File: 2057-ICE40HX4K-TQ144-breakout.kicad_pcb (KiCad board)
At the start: 2 copper layers, 99.1 x 66 mm, 61 parts, among them J1 Conn_02x30_Odd_Even, J2 Conn_02x30_Odd_Even, J3 RaspberryPI-B+header, J4 0548190519, J5 RaspberryPI-B+header, J6 Conn_02x07_Odd_Even, J7 Conn_02x01, U1 ICE40HX4K-TQ144, U2 AZ1117CH-3.3TRG1, U3 AZ1117CH-1.2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

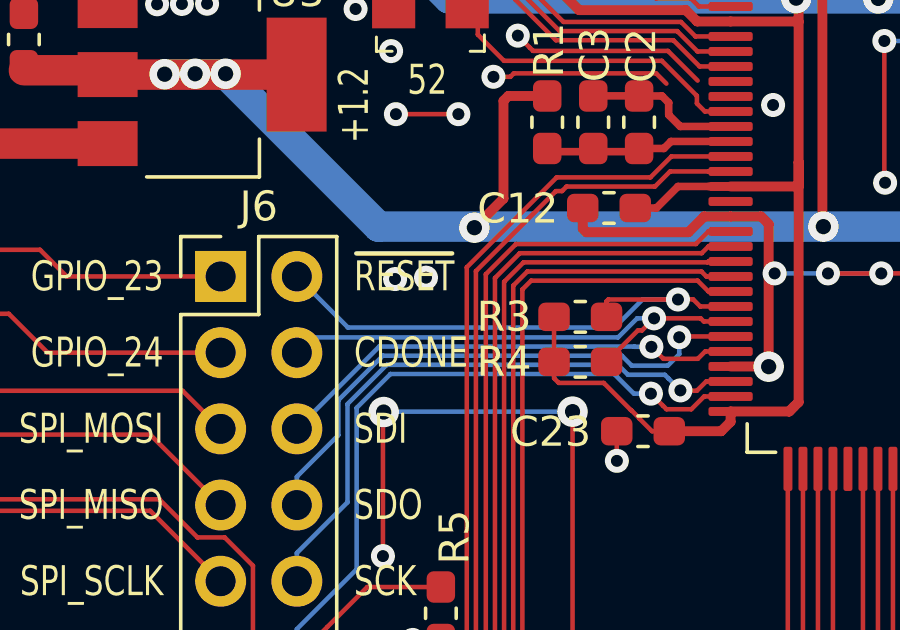
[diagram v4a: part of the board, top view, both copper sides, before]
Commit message: swap ~reset & cdone on silkscreen :-/
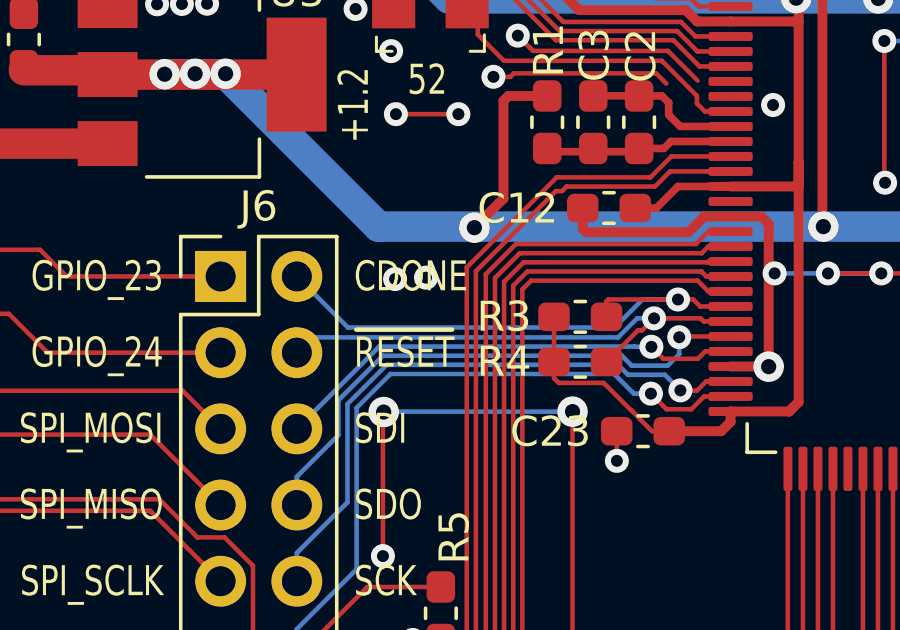
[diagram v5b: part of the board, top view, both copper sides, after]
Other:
- board text added: "~RESET"
- board text removed: "~RESET~"
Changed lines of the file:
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@@
-(kicad_pcb (version 20171130) (host pcbnew 5.1.5-52549c5~84~ubuntu18.04.1)
+(kicad_pcb (version 20171130) (host pcbnew 5.1.5+dfsg1-2build2)
   (general
     (thickness 1.6)
@@
     (effects (font (size 1 0.762) (thickness 0.15)))
   )
-  (gr_text CDONE (at 69.215 77.47) (layer F.SilkS)
+  (gr_text CDONE (at 69.215 74.93) (layer F.SilkS)
     (effects (font (size 1 0.762) (thickness 0.15)) (justify left))
   )
-  (gr_text ~RESET~ (at 69.215 74.93) (layer F.SilkS)
+  (gr_text ~RESET (at 69.215 77.47) (layer F.SilkS)
     (effects (font (size 1 0.762) (thickness 0.15)) (justify left))
   )

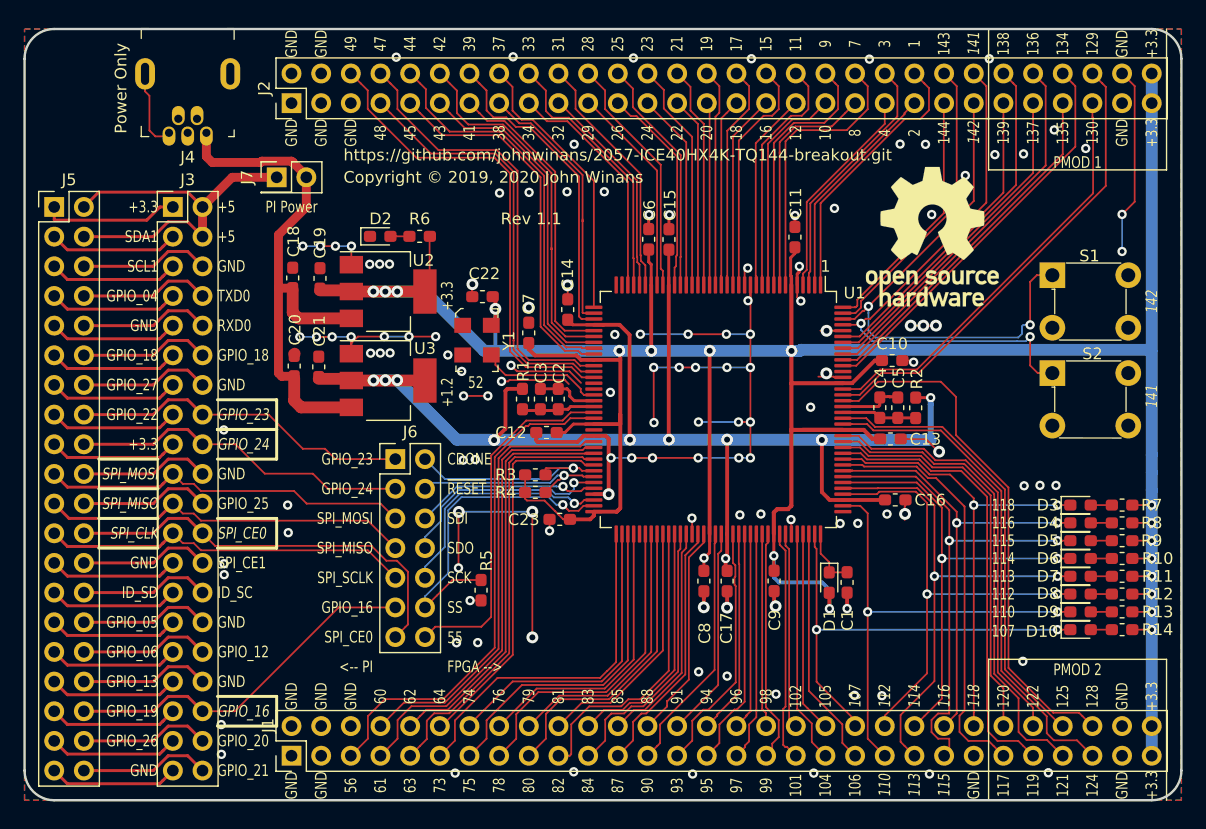
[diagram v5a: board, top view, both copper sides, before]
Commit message: Add FLASH, SD, gnd testpoints for Rev 2.0
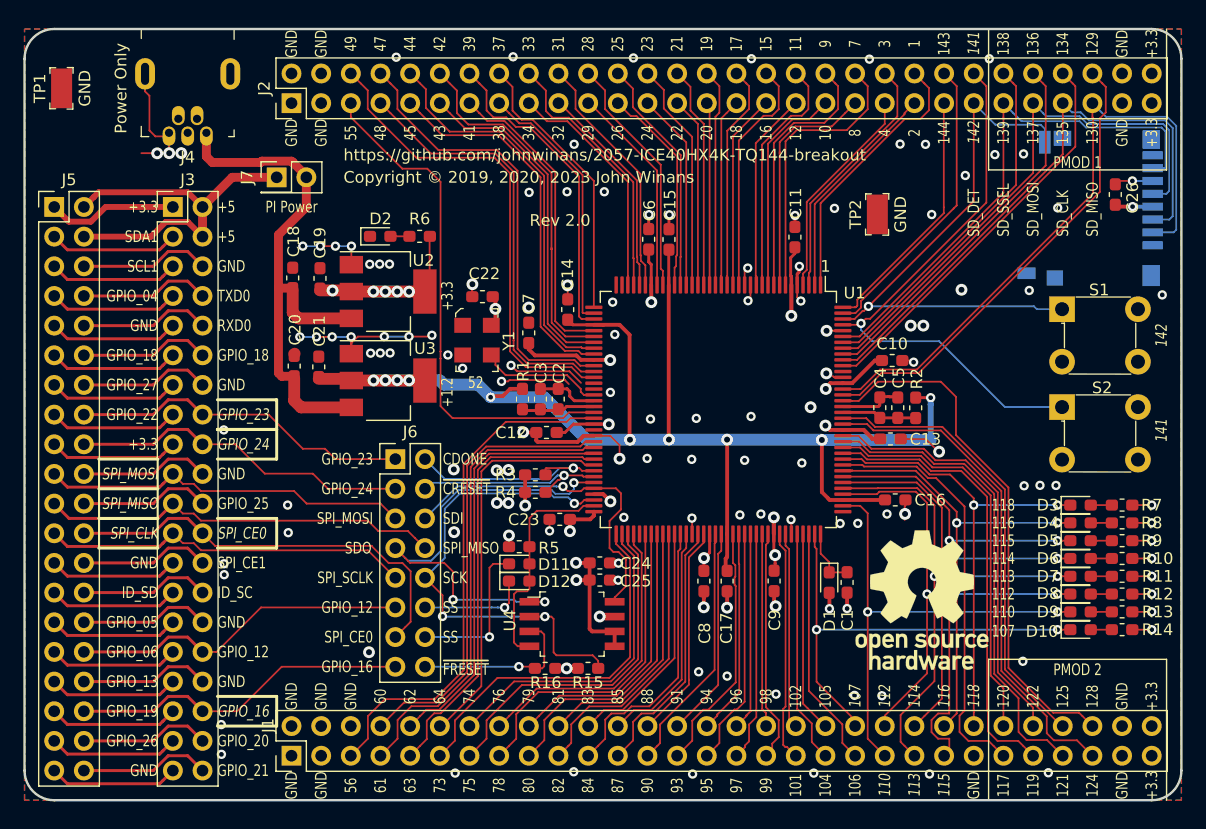
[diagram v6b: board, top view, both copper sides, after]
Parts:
- added C24: .1uF, Capacitor_SMD:C_0603_1608Metric_Pad1.05x0.95mm_HandSolder, F.Cu at (82.3, 83.8)
- added C25: 4.7uF, Capacitor_SMD:C_0603_1608Metric_Pad1.05x0.95mm_HandSolder, F.Cu at (82.3, 85.3)
- added C26: .1uF, Capacitor_SMD:C_0603_1608Metric_Pad1.05x0.95mm_HandSolder, F.Cu at (126.4, 52.3)
- added D11: 1N4448WSF-7, Diode_SMD:D_0603_1608Metric_Pad1.05x0.95mm_HandSolder, F.Cu at (75.4, 83.9)
- added D12: 1N4448WSF-7, Diode_SMD:D_0603_1608Metric_Pad1.05x0.95mm_HandSolder, F.Cu at (75.4, 85.4)
- added J8: Micro_SD_Card_Det, jb-footprint:microSD_HC_Hirose_DM3D-SF-bigpad, B.Cu at (124.3, 53.4)
- added R15: 10K, Resistor_SMD:R_0603_1608Metric_Pad1.05x0.95mm_HandSolder, F.Cu at (81.3, 92.8)
- added R16: 10K, Resistor_SMD:R_0603_1608Metric_Pad1.05x0.95mm_HandSolder, F.Cu at (77.6, 92.8)
- added TP1: RCW-0C, digikey-footprints:PROBE_PAD_1206, F.Cu at (36.2, 43.2)
- added TP2: RCW-0C, digikey-footprints:PROBE_PAD_1206, F.Cu at (106.0, 54.0)
- added U4: AT45DB161D-SU, digikey-footprints:SOIC-8_W5.6mm, F.Cu at (79.9, 89.0)
- D1: value D_ALT -> 1N4448WSF-7
- J6: value Conn_02x07_Odd_Even -> Conn_02x08_Odd_Even; footprint Connector_PinHeader_2.54mm:PinHeader_2x07_P2.54mm_Vertical -> Connector_PinHeader_2.54mm:PinHeader_2x08_P2.54mm_Vertical
- moved LOGO1 31.1 mm to (109.9, 87.0)
- moved R5 4.96 mm to (75.4, 82.4), turned to 180 degrees
- moved S2 3.03 mm to (121.9, 70.5)
- moved S1 3.03 mm to (121.9, 62.1)
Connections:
- J2 pad 5: GND -> /IOB_91
- J6 pad 11: /GPIO16 -> /GPIO12
- J6 pad 12: /IOB_108_SS -> /J6_GPIO12
- J6 pad 14: /IOB_91 -> /J6_CE0
- J6 pad 7: /SPI_MISO -> /IOB_105_SDO
- J6 pad 8: /IOB_105_SDO -> /SPI_MISO
- R5 pad 1: GND -> /IOB_108_SS
- R5 pad 2: /IOB_108_SS -> +3V3
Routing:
- net +3V3: track 288.2 -> 99.3 mm, vias 19 -> 31
- net GND: track 272.8 -> 183.8 mm, vias 129 -> 122
- net /IOB_107_SCK: track 20.4 -> 42.9 mm, vias 1 -> 3
- net /IOB_105_SDO: track 18.6 -> 40.4 mm, vias 1 -> 3
- net /IOT_213: track 30.5 -> 50.2 mm
- net /IOT_215: track 28.5 -> 47.8 mm
- net /IOT_217: track 26.5 -> 45.6 mm
- net /IOT_206: track 36.1 -> 55.1 mm
- net /GPIO12: track 11.2 -> 29.3 mm
- net /~FRESET~: track 0.00 -> 14.4 mm, vias 0 -> 1
- net /IOB_91: track 30.5 -> 44.1 mm
- net /IOB_106_SDI: track 15.9 -> 29.3 mm
- net /J6_CE0: track 0.00 -> 13.3 mm, vias 0 -> 1
- net /IOB_108_SS: track 28.5 -> 19.1 mm, vias 1 -> 0
- net /J6_GPIO12: track 0.00 -> 9.25 mm, vias 0 -> 1
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- added copper zone on In2.Cu, net +3V3
- added copper zone on In1.Cu, net GND
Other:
- copper layers 2 -> 4
- board text added: "Copyright © 2019, 2020, 2023 John Winans"
- board text added: "Rev 2.0"
- board text added: "SD_CLK"
- board text added: "SD_DET"
- board text added: "SD_MISO"
- board text added: "SD_MOSI"
- board text added: "SD_SSEL"
- board text added: "https://github.com/johnwinans/2057-ICE40HX4K-TQ144-breakout"
- board text added: "~CRESET"
- board text added: "~FRESET"
- board text removed: "<-- PI"
- board text removed: "Copyright © 2019, 2020 John Winans"
- board text removed: "FPGA -->"
- board text removed: "Rev 1.1"
- board text removed: "https://github.com/johnwinans/2057-ICE40HX4K-TQ144-breakout.git"
- board text removed: "~RESET"

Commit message: Change filter caps to 0805 Silk correct GPIO18 Silk mark GPIO12 Added C27
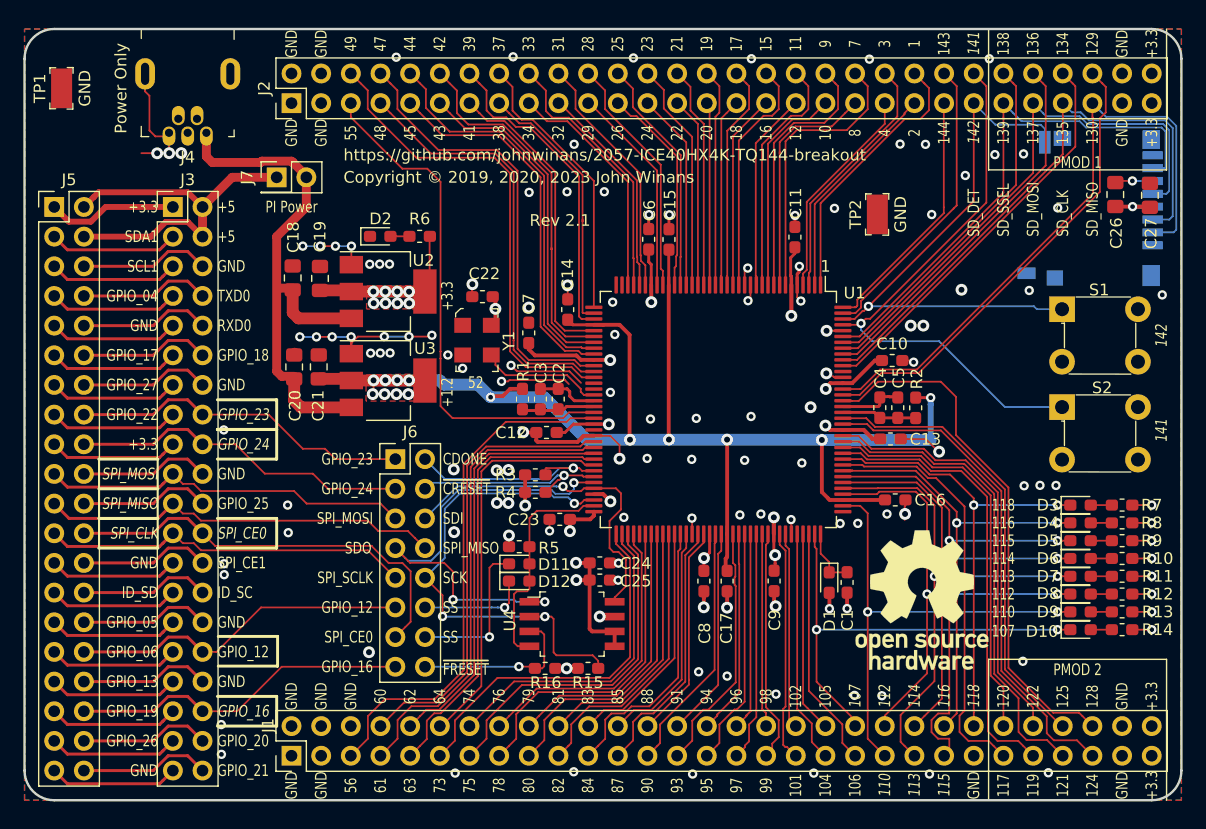
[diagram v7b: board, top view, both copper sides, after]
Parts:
- added C27: 22uF, Capacitor_SMD:C_0805_2012Metric_Pad1.15x1.40mm_HandSolder, F.Cu at (129.4, 52.3)
- C18, C19, C20, C21, C26: footprint Capacitor_SMD:C_0603_1608Metric_Pad1.05x0.95mm_HandSolder -> Capacitor_SMD:C_0805_2012Metric_Pad1.15x1.40mm_HandSolder
- moved C20 0.07 mm to (56.1, 67.0)
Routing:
- net +3V3: track 99.3 -> 103.8 mm, vias 31 -> 34
- net +1V2: track 119.3 -> 123.6 mm, vias 10 -> 14
- added copper zone on F.Cu, net +1V2
- added copper zone on F.Cu, net +3V3
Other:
- board text added: "GPIO_17"
- board text added: "Rev 2.1"
- board text removed: "Rev 2.0"

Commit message: Change USB connector, re-route SD & buttons
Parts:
- added R17: 5.1K, Resistor_SMD:R_0603_1608Metric_Pad1.05x0.95mm_HandSolder, F.Cu at (50.8, 49.4)
- added R18: 5.1K, Resistor_SMD:R_0603_1608Metric_Pad1.05x0.95mm_HandSolder, F.Cu at (43.9, 49.3)
- J4: value 0548190519 -> USB4105-GF-A; footprint digikey-footprints:USB_Mini_B_Female_548190519 -> jb-footprint:USB_C_Receptacle_HRO_TYPE-C-31-M-12
- moved J4 5.27 mm to (47.5, 41.7), turned to 180 degrees
- moved J7 1.78 mm to (54.6, 52.6)
- turned TP2 to 180 degrees
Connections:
- J8 pad 10: GND -> /IOT_192
- J8 pad 2: /IOT_206 -> /IOT_174
- J8 pad 3: /IOT_213 -> /IOT_178
- J8 pad 5: /IOT_215 -> /IOT_191
- J8 pad 7: /IOT_217 -> /IOT_181
- J8 pad 9: /IOT_220 -> GND
- S1 pad 1: /IOT_220 -> /IOR_161
- S2 pad 1: /IOT_219 -> /IOR_165
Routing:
- net /IOT_181: track 40.7 -> 104.5 mm
- net /IOT_192: track 38.8 -> 99.1 mm
- net /IOT_174: track 36.0 -> 94.7 mm
- net /IOT_191: track 43.0 -> 101.0 mm
- net /IOT_178: track 38.7 -> 96.7 mm
- net /IOR_161: track 16.8 -> 56.8 mm, vias 0 -> 1
- net /IOR_165: track 17.2 -> 47.5 mm, vias 0 -> 1
- net /IOT_220: track 48.6 -> 23.8 mm, vias 1 -> 0
- net /IOT_219: track 48.6 -> 28.1 mm, vias 1 -> 0
- net /IOT_213: track 50.2 -> 30.5 mm
- net /IOT_215: track 47.8 -> 28.5 mm
- net /IOT_217: track 45.6 -> 26.5 mm
- net /IOT_206: track 55.1 -> 36.1 mm
- net GND: track 183.8 -> 171.3 mm, vias 122 -> 129
- net +5V: track 46.3 -> 53.5 mm
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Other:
- board text added: "Rev 3.0"
- board text removed: "Rev 2.1"
